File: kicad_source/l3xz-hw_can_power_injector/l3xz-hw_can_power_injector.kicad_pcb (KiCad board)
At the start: 2 copper layers, 46 x 51 mm, 28 parts, among them CN1 Conn_01x02, CN2 Conn_01x04, CN3 Conn_01x04, CN4 Conn_01x02, CN5 Conn_01x04, CN6 Conn_01x04, U1 RAA211650

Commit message: added LED
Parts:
- added D3: LED_Small, LED_SMD:LED_0603_1608Metric, F.Cu at (129.0, 90.0)
- added R4: 2k2, Resistor_SMD:R_0603_1608Metric, F.Cu at (125.0, 90.0)
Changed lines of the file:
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@@
   (net 18 "/CAN2H")
   (net 19 "/CAN2L")
+  (net 20 "Net-(D3-Pad2)")
   (footprint "Connector_JST:JST_GH_BM04B-GHS-TBT_1x04-1MP_P1.25mm_Vertical" (layer "F.Cu")
     (at 134 107.5 -90)
@@
       (net 2 "GND") (pintype "passive"))
     (model "${KICAD6_3DMODEL_DIR}/Resistor_SMD.3dshapes/R_0603_1608Metric.wrl"
+      (offset (xyz 0 0 0))
+      (scale (xyz 1 1 1))
+      (rotate (xyz 0 0 0))
+    )
+  )
+  (footprint "LED_SMD:LED_0603_1608Metric" (layer "F.Cu")
+    (at 129 90 180)
+    (descr "LED SMD 0603 (1608 Metric), square (rectangular) end terminal, IPC_7351 nominal, (Body size source: http://www.tortai-tech.com/upload/download/2011102023233369053.pdf), generated with kicad-footprint-generator")
+    (tags "LED")
+    (property "Sheetfile" "Datei: l3xz-hw_can_power_injector.kicad_sch")
+    (property "Sheetname" "")
+    (attr smd)
+    (fp_text reference "D3" (at 0 -1.43) (layer "F.SilkS")
+      (effects (font (size 1 1) (thickness 0.15)))
+    )
+    (fp_text value "LED_Small" (at 0 1.43) (layer "F.Fab")
+      (effects (font (size 1 1) (thickness 0.15)))
+    )
+    (fp_text user "${REFERENCE}" (at 0 0) (layer "F.Fab")
+      (effects (font (size 0.4 0.4) (thickness 0.06)))
+    )
+    (fp_line (start 0.8 -0.735) (end -1.485 -0.735) (layer "F.SilkS") (width 0.12))
+    (fp_line (start -1.485 0.735) (end 0.8 0.735) (layer "F.SilkS") (width 0.12))
+    (fp_line (start -1.485 -0.735) (end -1.485 0.735) (layer "F.SilkS") (width 0.12))
+    (fp_line (start -1.48 -0.73) (end 1.48 -0.73) (layer "F.CrtYd") (width 0.05))
+    (fp_line (start 1.48 0.73) (end -1.48 0.73) (layer "F.CrtYd") (width 0.05))
+    (fp_line (start -1.48 0.73) (end -1.48 -0.73) (layer "F.CrtYd") (width 0.05))
+    (fp_line (start 1.48 -0.73) (end 1.48 0.73) (layer "F.CrtYd") (width 0.05))
+    (fp_line (start 0.8 0.4) (end 0.8 -0.4) (layer "F.Fab") (width 0.1))
+    (fp_line (start 0.8 -0.4) (end -0.5 -0.4) (layer "F.Fab") (width 0.1))
+    (fp_line (start -0.8 -0.1) (end -0.8 0.4) (layer "F.Fab") (width 0.1))
+    (fp_line (start -0.5 -0.4) (end -0.8 -0.1) (layer "F.Fab") (width 0.1))
+    (fp_line (start -0.8 0.4) (end 0.8 0.4) (layer "F.Fab") (width 0.1))
+    (pad "1" smd roundrect (at -0.7875 0 180) (size 0.875 0.95) (layers "F.Cu" "F.Paste" "F.Mask") (roundrect_rratio 0.25)
+      (net 2 "GND") (pinfunction "K") (pintype "passive"))
+    (pad "2" smd roundrect (at 0.7875 0 180) (size 0.875 0.95) (layers "F.Cu" "F.Paste" "F.Mask") (roundrect_rratio 0.25)
+      (net 20 "Net-(D3-Pad2)") (pinfunction "A") (pintype "passive"))
+    (model "${KICAD6_3DMODEL_DIR}/LED_SMD.3dshapes/LED_0603_1608Metric.wrl"
       (offset (xyz 0 0 0))
       (scale (xyz 1 1 1))
@@
       (offset (xyz 0 0 0))
       (scale (xyz 1 1 1))
+      (rotate (xyz 0 0 0))
+    )
+  )
+  (footprint "Resistor_SMD:R_0603_1608Metric" (layer "F.Cu")
+    (at 125 90)
+    (descr "Resistor SMD 0603 (1608 Metric), square (rectangular) end terminal, IPC_7351 nominal, (Body size source: IPC-SM-782 page 72, https://www.pcb-3d.com/wordpress/wp-content/uploads/ipc-sm-782a_amendment_1_and_2.pdf), generated with kicad-footprint-generator")
+    (tags "resistor")
+    (property "Sheetfile" "Datei: l3xz-hw_can_power_injector.kicad_sch")
+    (property "Sheetname" "")
+    (attr smd)
+    (fp_text reference "R4" (at 0 -1.43) (layer "F.SilkS")
+      (effects (font (size 1 1) (thickness 0.15)))
+    )
+    (fp_text value "2k2" (at 0 1.43) (layer "F.Fab")
+      (effects (font (size 1 1) (thickness 0.15)))
+    )
+    (fp_text user "${REFERENCE}" (at 0 0) (layer "F.Fab")
+      (effects (font (size 0.4 0.4) (thickness 0.06)))
+    )
+    (fp_line (start -0.237258 0.5225) (end 0.237258 0.5225) (layer "F.SilkS") (width 0.12))
+    (fp_line (start -0.237258 -0.5225) (end 0.237258 -0.5225) (layer "F.SilkS") (width 0.12))
+    (fp_line (start -1.48 -0.73) (end 1.48 -0.73) (layer "F.CrtYd") (width 0.05))
+    (fp_line (start 1.48 0.73) (end -1.48 0.73) (layer "F.CrtYd") (width 0.05))
+    (fp_line (start -1.48 0.73) (end -1.48 -0.73) (layer "F.CrtYd") (width 0.05))
+    (fp_line (start 1.48 -0.73) (end 1.48 0.73) (layer "F.CrtYd") (width 0.05))
+    (fp_line (start -0.8 0.4125) (end -0.8 -0.4125) (layer "F.Fab") (width 0.1))
+    (fp_line (start 0.8 -0.4125) (end 0.8 0.4125) (layer "F.Fab") (width 0.1))
+    (fp_line (start -0.8 -0.4125) (end 0.8 -0.4125) (layer "F.Fab") (width 0.1))
+    (fp_line (start 0.8 0.4125) (end -0.8 0.4125) (layer "F.Fab") (width 0.1))
+    (pad "1" smd roundrect (at -0.825 0) (size 0.8 0.95) (layers "F.Cu" "F.Paste" "F.Mask") (roundrect_rratio 0.25)
+      (net 3 "VCC") (pintype "passive"))
+    (pad "2" smd roundrect (at 0.825 0) (size 0.8 0.95) (layers "F.Cu" "F.Paste" "F.Mask") (roundrect_rratio 0.25)
+      (net 20 "Net-(D3-Pad2)") (pintype "passive"))
+    (model "${KICAD6_3DMODEL_DIR}/Resistor_SMD.3dshapes/R_0603_1608Metric.wrl"
+      (offset (xyz 0 0 0))
+      (scale (xyz 1 1 1))

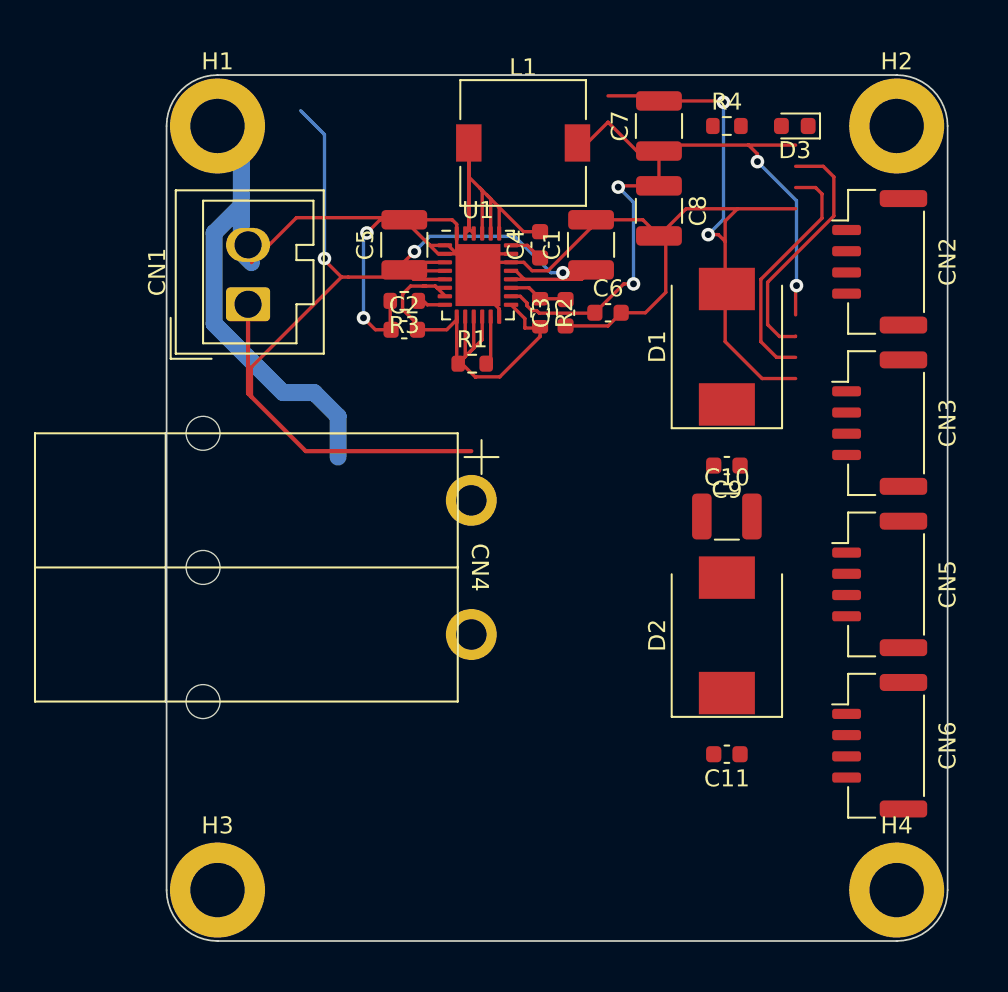
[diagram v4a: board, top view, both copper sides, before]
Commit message: added TVS diode and capacitors, updated layout
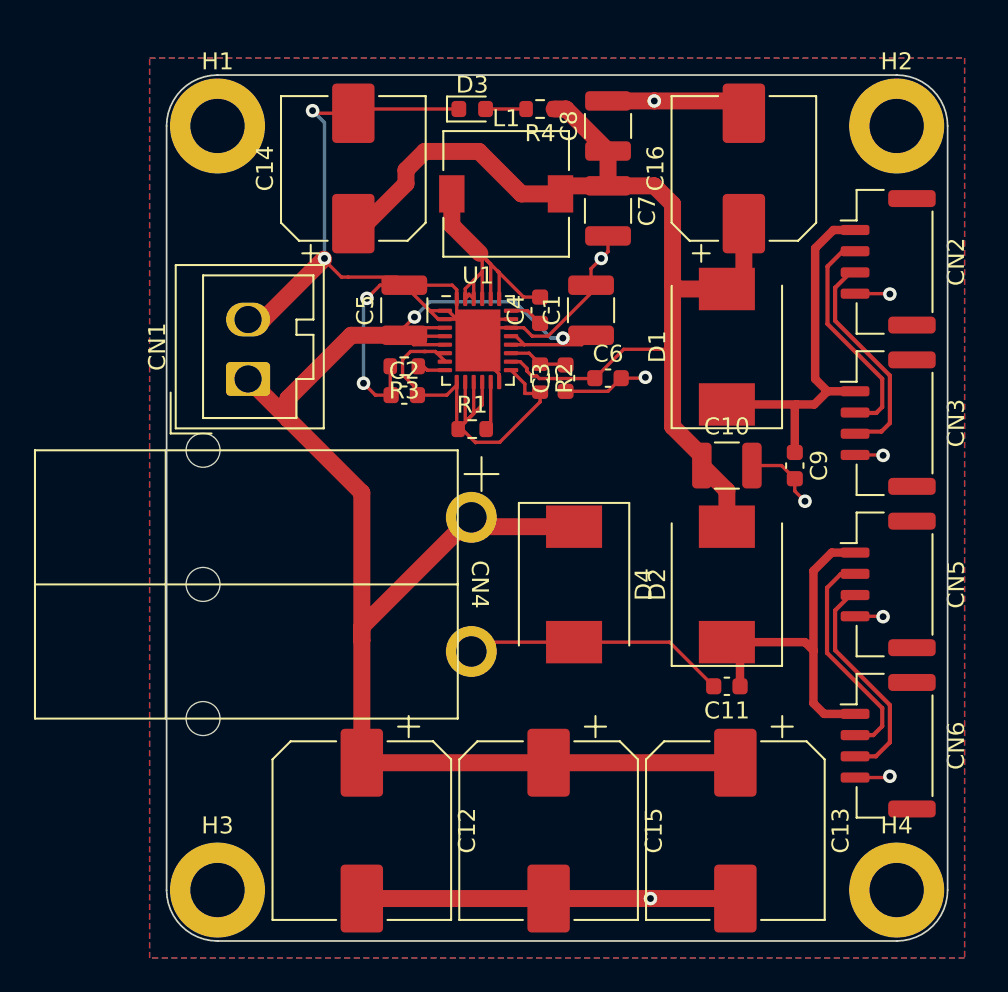
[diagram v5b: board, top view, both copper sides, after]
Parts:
- added C12: 100 uF / 50 V, Capacitor_SMD:CP_Elec_10x10, F.Cu at (103.5, 131.5)
- added C13: 100 uF / 50 V, Capacitor_SMD:CP_Elec_10x10, F.Cu at (125.5, 131.5)
- added C14: 470 uF / 10 V, Capacitor_SMD:CP_Elec_8x10, F.Cu at (103.0, 92.5)
- added C15: 100 uF / 50 V, Capacitor_SMD:CP_Elec_10x10, F.Cu at (114.5, 131.5)
- added C16: 470 uF / 10 V, Capacitor_SMD:CP_Elec_8x10, F.Cu at (126.0, 92.5)
- added D4: SMCJ40A, Diode_SMD:D_SMC, F.Cu at (116.0, 117.0)
- moved D3 19.0 mm to (110.0, 89.0), turned to 0 degrees
- moved R4 11.0 mm to (114.0, 89.0), turned to 180 degrees
- moved C7 5.83 mm to (118.0, 95.0), turned to -90 degrees
- moved C8 5.83 mm to (118.0, 90.0), turned to 90 degrees
- moved CN1 4.40 mm to (96.8, 104.9)
- moved C11 4.00 mm to (125.0, 123.0)
- moved C9 4.00 mm to (129.0, 110.0), turned to -90 degrees
- moved C1 3.85 mm to (117.0, 100.9)
- moved C2 3.85 mm to (106.0, 105.9)
- moved C3 3.85 mm to (115.5, 104.9)
- moved C4 3.85 mm to (114.0, 100.9)
- moved C5 3.85 mm to (106.0, 100.9)
- moved C6 3.85 mm to (118.0, 104.9)
- moved R1 3.85 mm to (110.0, 107.9)
- moved R2 3.85 mm to (114.0, 104.9)
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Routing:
- net +BATT: track 70.4 -> 100.4 mm, vias 3 -> 2
- net (no net): track 29.1 -> 0.00 mm
- net VCC: track 44.4 -> 67.7 mm, vias 4 -> 0
- net /CAN1VCC: track 0.00 -> 22.3 mm
- net /CAN2VCC: track 0.00 -> 21.6 mm
- net /CAN1H: track 0.00 -> 13.4 mm
- net /CAN2H: track 0.00 -> 13.3 mm
- net /CAN1L: track 0.00 -> 13.2 mm
- net /CAN2L: track 0.00 -> 13.0 mm
- net /PHASE: track 25.2 -> 19.4 mm
- net GND: track 131.3 -> 134.5 mm, vias 4 -> 13
- net Net-(D3-Pad2): track 0.00 -> 2.39 mm
- added copper zone on B.Cu, net GND
- added copper zone on F.Cu, net GND

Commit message: changed connector for input, added connector for VCC
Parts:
- added CN7: Conn_01x02, Connector_PinHeader_2.54mm:PinHeader_1x02_P2.54mm_Vertical, F.Cu at (119.5, 109.8)
- CN1: footprint Connector_Wago:Wago_734-132_1x02_P3.50mm_Vertical -> Connector_Phoenix_MC:PhoenixContact_MC_1,5_2-G-3.5_1x02_P3.50mm_Horizontal
- moved CN1 4.74 mm to (100.1, 101.5), turned to -90 degrees
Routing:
- net GND: track 134.5 -> 143.8 mm
- net VCC: track 67.7 -> 70.9 mm
- net +BATT: track 100.4 -> 97.9 mm

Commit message: updated and set analog values of switching regulator
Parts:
- added C17: 10nF, Capacitor_SMD:C_0603_1608Metric, F.Cu at (106.0, 105.7)
- added R5: 120k, Resistor_SMD:R_0603_1608Metric, F.Cu at (108.7, 107.5)
- added R6: 20k, Resistor_SMD:R_0603_1608Metric, F.Cu at (110.2, 107.5)
- moved R1 1.83 mm to (111.8, 107.5), turned to 90 degrees
- moved C2 1.35 mm to (106.0, 107.2)
- turned L1 to 90 degrees
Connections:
- U1 pad 11: /AVCC -> /FB
- U1 pad 9: /AVCC -> /SS
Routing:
- net VCC: track 70.9 -> 84.3 mm, vias 0 -> 2
- net /PHASE: track 19.4 -> 25.8 mm
- net GND: track 143.8 -> 149.5 mm, vias 13 -> 18
- net /FB: track 0.00 -> 3.14 mm
- net /SS: track 0.00 -> 2.76 mm
- net /AVCC: track 29.7 -> 27.3 mm
- net /PG: track 2.88 -> 1.89 mm

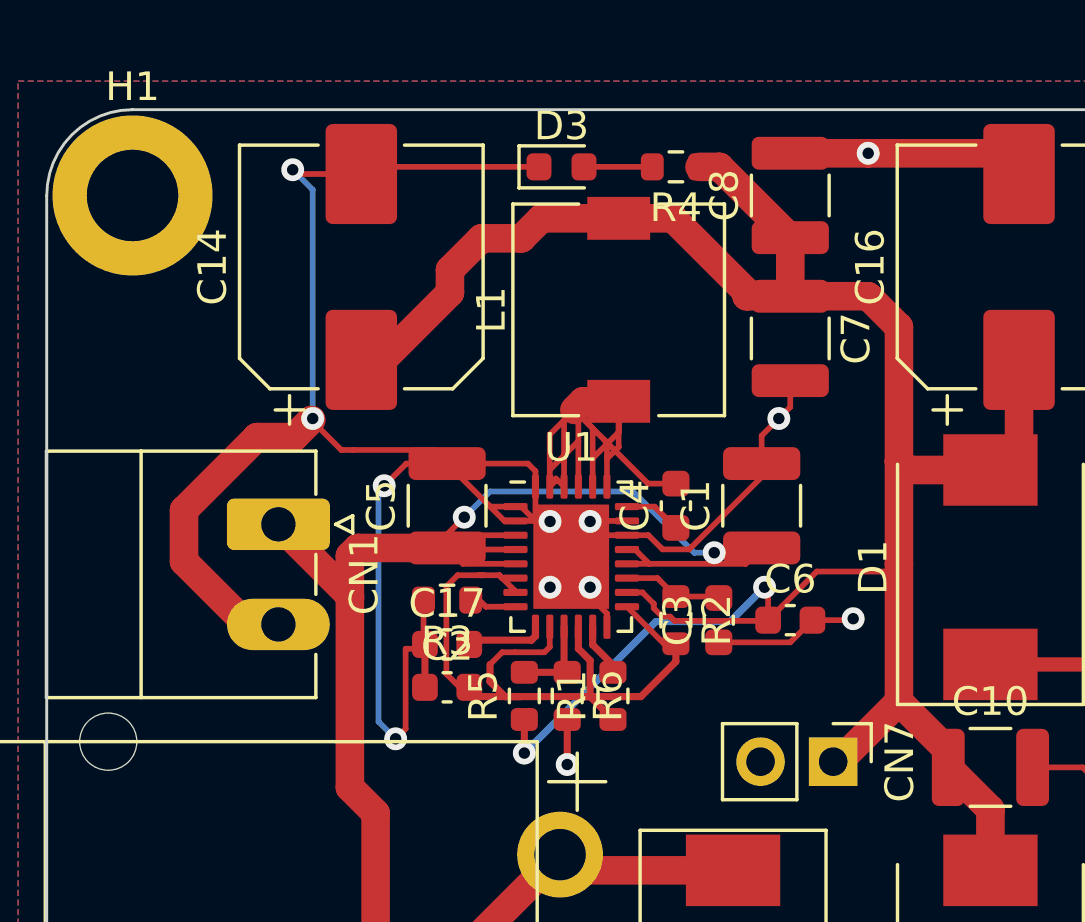
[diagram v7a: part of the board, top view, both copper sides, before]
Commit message: added enable on VIN
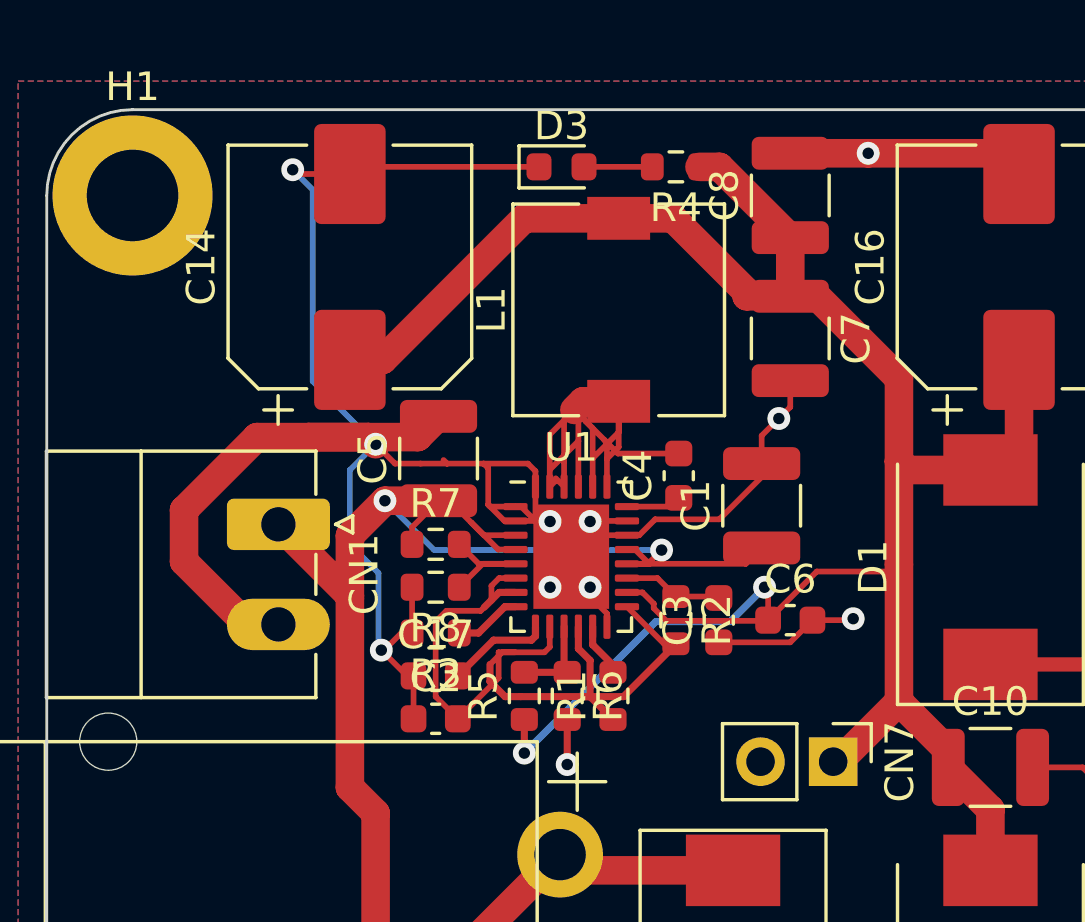
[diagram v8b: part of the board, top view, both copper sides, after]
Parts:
- added R7: 120k, Resistor_SMD:R_0603_1608Metric, F.Cu at (105.6, 102.2)
- added R8: 20k, Resistor_SMD:R_0603_1608Metric, F.Cu at (105.6, 103.7)
- C2: value C_Small -> 1 uF
- C3: value C_Small -> 2.2 uF
- C4, C6: value C_Small -> 100 nF
- L1: value L_Small -> 10 uH
- R1: value R_Small -> 10k
- R2: value R_Small -> 1R
- R3: value R_Small -> 30k
- moved C5 1.68 mm to (105.7, 99.2)
- moved R3 1.22 mm to (105.6, 105.3)
- moved C17 1.17 mm to (105.6, 106.8)
- moved C2 1.17 mm to (105.6, 108.3)
- moved C4 1.06 mm to (114.1, 99.8)
- moved C14 0.40 mm to (102.6, 92.5)
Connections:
- U1 pad 5: +BATT -> /EN
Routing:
- net /EN: track 0.00 -> 4.55 mm
- net +BATT: track 97.9 -> 95.6 mm
- net /AVCC: track 27.3 -> 29.2 mm
- net VCC: track 84.3 -> 82.8 mm
- net GND: track 149.5 -> 150.5 mm, vias 18 -> 17
- net /SS: track 2.76 -> 3.62 mm
- net /SET: track 1.78 -> 2.35 mm
